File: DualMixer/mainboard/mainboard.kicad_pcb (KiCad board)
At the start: 2 copper layers, 35.6 x 107.9 mm, 44 parts, among them J12 Conn_02x05_Odd_Even, J13 Conn_01x03_Male, J5 Conn_02x07_Odd_Even, U1 TL074, U2 TL074, U3 TL074

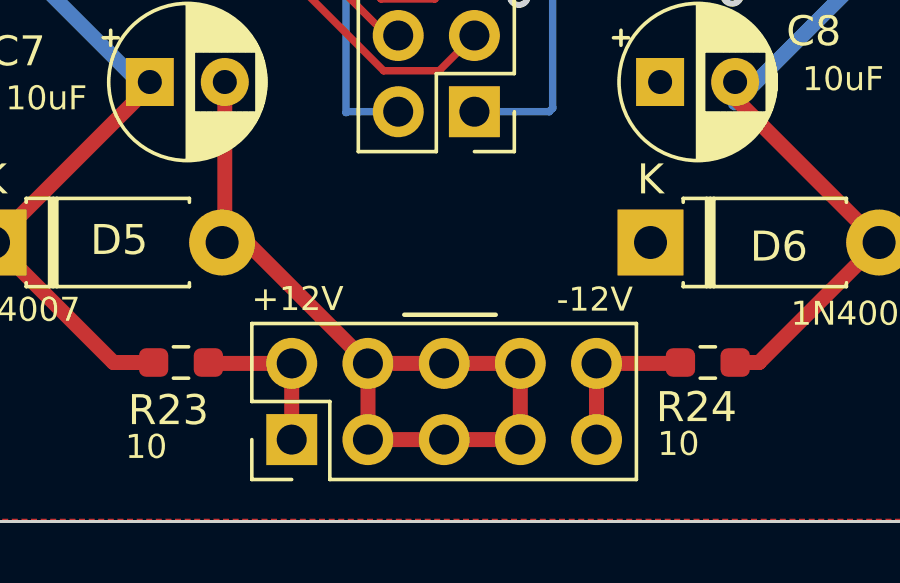
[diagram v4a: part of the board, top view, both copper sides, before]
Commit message: Add M3 mount for mechanical stability, and update power
This time for the DualMixer as well, it could do with extra supports
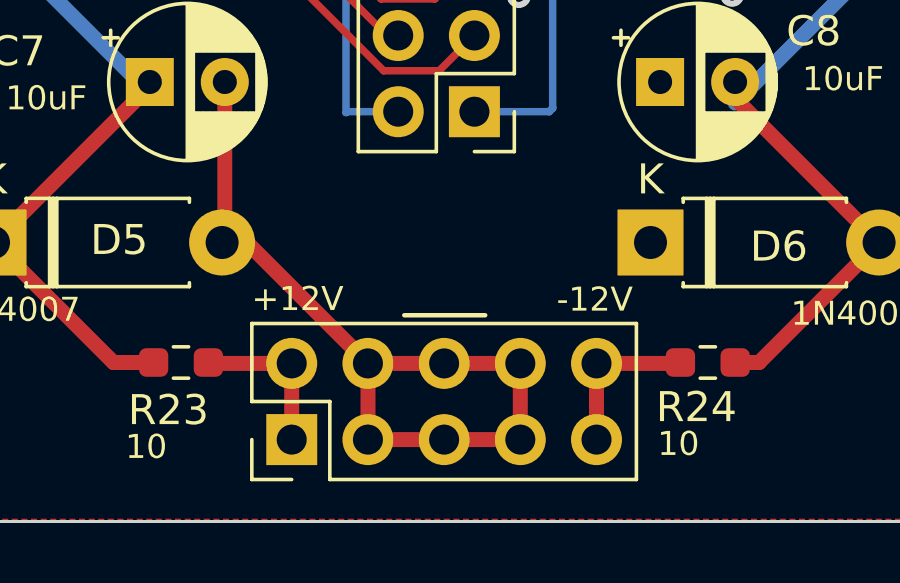
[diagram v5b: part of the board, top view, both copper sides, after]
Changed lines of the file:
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@@
     )
   )
+  (gr_line (start 74.125 146.125) (end 87.35 146.05) (layer "B.SilkS") (width 0.15))
+  (gr_line (start 79.6 146.4) (end 82 146.4) (layer "B.SilkS") (width 0.15))
   (gr_line (start 74.57 102.73) (end 75.45 102.09) (layer "F.SilkS") (width 0.15))
   (gr_line (start 90.59 51.81) (end 90.04 54.54) (layer "F.SilkS") (width 0.15))
@@
   (gr_line (start 90.04 54.5) (end 89.58 55.18) (layer "F.SilkS") (width 0.15))
   (gr_line (start 90.93 50.5) (end 90.59 51.81) (layer "F.SilkS") (width 0.15))
-  (gr_line (start 79.502 140.208) (end 82.55 140.208) (layer "F.SilkS") (width 0.15))
+  (gr_line (start 79.502 140.225) (end 82.2 140.225) (layer "F.SilkS") (width 0.15))
   (gr_rect (start 62.81 147.1) (end 98.37 39.15) (layer "Edge.Cuts") (width 0.1) (fill none))
+  (gr_text "-12V" (at 86.3 139.775) (layer "B.SilkS")
+    (effects (font (size 1 1) (thickness 0.15)) (justify mirror))
+  )
+  (gr_text "+12V" (at 76.425 139.725) (layer "B.SilkS")
+    (effects (font (size 1 1) (thickness 0.15)) (justify mirror))
+  )
   (gr_text "+12V" (at 75.946 139.680467) (layer "F.SilkS")
     (effects (font (size 0.8 0.8) (thickness 0.15)))

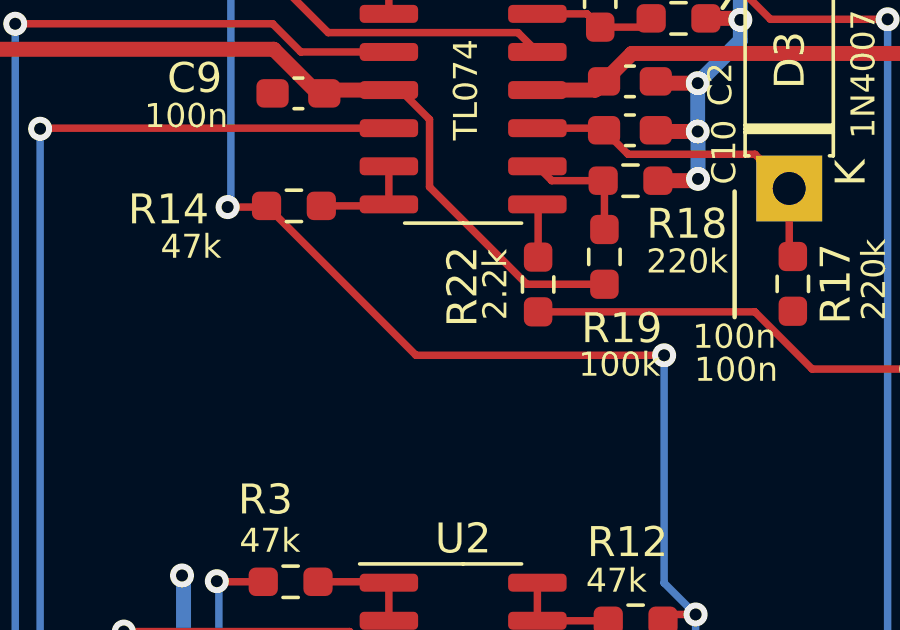
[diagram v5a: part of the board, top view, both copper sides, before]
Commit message: Add extra ioboard + mainboard holes securing connection
So the two boards don't separate after installation.
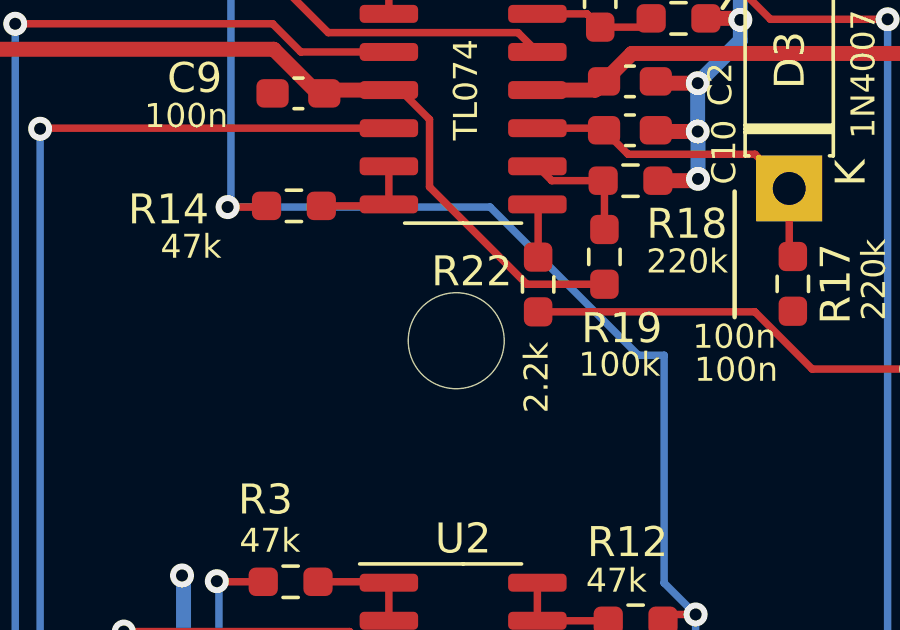
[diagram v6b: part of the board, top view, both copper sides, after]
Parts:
- added REF**: MountingHole_3.2mm_M3_NoCourt, Library:MountingHole_3.2mm_M3_NoCourt, F.Cu at (80.7, 66.3)
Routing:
- net Net-(R11-Pad2): track 54.1 -> 55.4 mm, vias 5 -> 4
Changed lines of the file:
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@@
     )
+  )
+  (footprint "Library:MountingHole_3.2mm_M3_NoCourt" (layer "F.Cu")
+    (at 80.7 66.275)
+    (descr "Mounting Hole 3.2mm, no annular, M3")
+    (tags "mounting hole 3.2mm no annular m3")
+    (attr exclude_from_pos_files exclude_from_bom)
+    (fp_text reference "REF**" (at 0 -4.2) (layer "F.SilkS") hide
+      (effects (font (size 1 1) (thickness 0.15)))
+    )
+    (fp_text value "MountingHole_3.2mm_M3_NoCourt" (at 0 4.2) (layer "F.Fab")
+      (effects (font (size 1 1) (thickness 0.15)))
+    )
+    (fp_text user "${REFERENCE}" (at 0 0) (layer "F.Fab")
+      (effects (font (size 1 1) (thickness 0.15)))
+    )
+    (fp_circle (center 0 0) (end 1.61 0) (layer "F.CrtYd") (width 0.05) (fill none))
+    (pad "" np_thru_hole circle (at 0 0) (size 3.2 3.2) (drill 3.2) (layers *.Cu *.Mask))
   )
   (footprint "Diode_THT:D_DO-41_SOD81_P7.62mm_Horizontal" (layer "F.Cu")
@@
     (property "Sheetname" "")
     (attr smd)
-    (fp_text reference "R22" (at 0.07 2.52 90) (layer "F.SilkS")
-      (effects (font (size 1 1) (thickness 0.15)))
-    )
-    (fp_text value "2.2k" (at 0 1.43 90) (layer "F.SilkS")
+    (fp_text reference "R22" (at -0.435 2.21 180) (layer "F.SilkS")
+      (effects (font (size 1 1) (thickness 0.15)))
+    )
+    (fp_text value "2.2k" (at 3.1 0.055 90) (layer "F.SilkS")
       (effects (font (size 0.8 0.8) (thickness 0.15)))
     )
@@
   (segment (start 87.7025 82.06) (end 88.81 82.06) (width 0.25) (layer "F.Cu") (net 29))
   (segment (start 76.4325 56.005) (end 82.76 56.005) (width 0.25) (layer "F.Cu") (net 29))
-  (segment (start 74.3775 61.78) (end 79.3575 66.76) (width 0.25) (layer "F.Cu") (net 29))
   (segment (start 88.68 75.4) (end 87.8025 75.4) (width 0.25) (layer "F.Cu") (net 29))
   (segment (start 73.08 61.82) (end 74.3375 61.82) (width 0.25) (layer "F.Cu") (net 29))
   (segment (start 87.8025 75.4) (end 87.5925 75.61) (width 0.25) (layer "F.Cu") (net 29))
   (segment (start 74.4775 54.05) (end 76.4325 56.005) (width 0.25) (layer "F.Cu") (net 29))
-  (segment (start 79.3575 66.76) (end 87.63 66.76) (width 0.25) (layer "F.Cu") (net 29))
   (segment (start 74.4775 54.05) (end 73.26 54.05) (width 0.25) (layer "F.Cu") (net 29))
   (segment (start 82.76 56.005) (end 83.405 56.65) (width 0.25) (layer "F.Cu") (net 29))
   (segment (start 88.81 82.06) (end 88.87 82.12) (width 0.25) (layer "F.Cu") (net 29))
   (via (at 73.08 61.82) (size 0.8) (drill 0.4) (layers "F.Cu" "B.Cu") (net 29))
-  (via (at 87.63 66.76) (size 0.8) (drill 0.4) (layers "F.Cu" "B.Cu") (net 29))
   (via (at 88.68 75.4) (size 0.8) (drill 0.4) (layers "F.Cu" "B.Cu") (net 29))
   (via (at 88.87 82.12) (size 0.8) (drill 0.4) (layers "F.Cu" "B.Cu") (net 29))
   (via (at 73.19 53.98) (size 0.8) (drill 0.4) (layers "F.Cu" "B.Cu") (net 29))
   (segment (start 87.63 66.76) (end 87.63 74.35) (width 0.25) (layer "B.Cu") (net 29))
+  (segment (start 86.771146 66.76) (end 87.63 66.76) (width 0.25) (layer "B.Cu") (net 29))
   (segment (start 88.68 81.93) (end 88.68 75.4) (width 0.25) (layer "B.Cu") (net 29))
+  (segment (start 81.831146 61.82) (end 86.771146 66.76) (width 0.25) (layer "B.Cu") (net 29))
   (segment (start 87.63 74.35) (end 88.68 75.4) (width 0.25) (layer "B.Cu") (net 29))
+  (segment (start 73.08 61.82) (end 81.831146 61.82) (width 0.25) (layer "B.Cu") (net 29))
   (segment (start 88.87 82.12) (end 88.68 81.93) (width 0.25) (layer "B.Cu") (net 29))
   (segment (start 73.19 53.98) (end 73.19 61.71) (width 0.25) (layer "B.Cu") (net 29))

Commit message: Apply fixes for DualMixer rev1 module
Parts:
- R18, R7: value 220k -> 33k
- moved R22 7.94 mm to (90.1, 68.8), turned to 0 degrees
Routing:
- net Net-(R22-Pad1): track 1.77 -> 9.91 mm
- net /LEDB: track 87.6 -> 79.9 mm
- net +12V: track 169.6 -> 170.7 mm
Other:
- board text added: "DualMixer mainboard-v2"
- board text removed: "DualMixer mainboard-v1"
